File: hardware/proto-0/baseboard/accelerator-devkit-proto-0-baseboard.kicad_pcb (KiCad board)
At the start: 6 copper layers, 50 x 42 mm, 175 parts, among them J1 JTAG, J2 USB-C, J3 HDMI, J4 Qwiic I2C, J5 Pmod 1A, J6 Pmod 1B, J7 Display, J8 microSD-ST11-H, Q1 CSD13381F4, SW1 BUTTON1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

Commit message: Adding some ground stitch vias
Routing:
- net /SDRAM/~SDRAM_RESET: track 15.2 -> 13.3 mm
- net /SDRAM/SDRAM_D9: track 13.8 -> 14.4 mm
- net GND: vias 137 -> 148
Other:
- board text removed: "TODO: GND stitch vias"

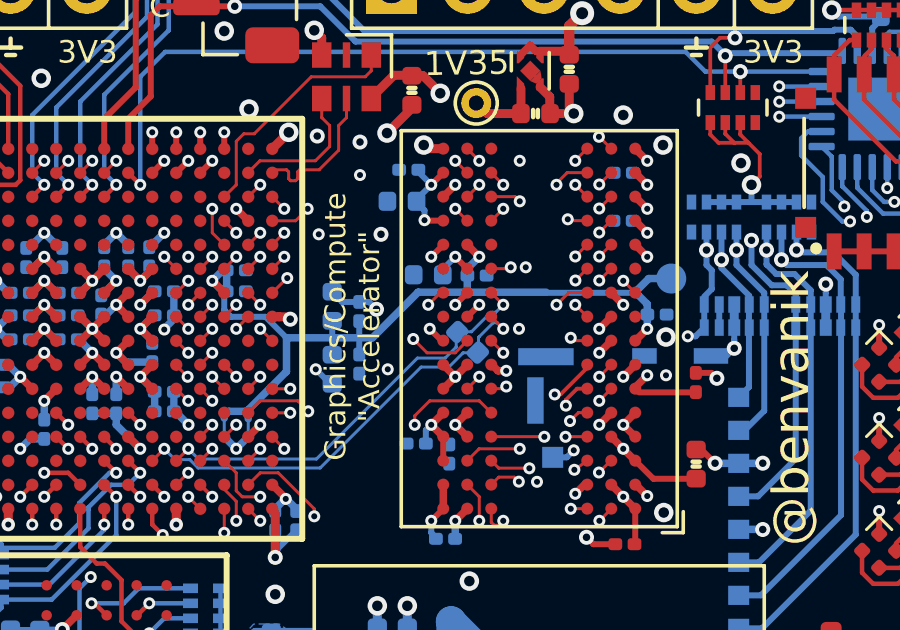
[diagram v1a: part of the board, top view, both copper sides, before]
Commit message: Thickening sDRAM_VREF traces
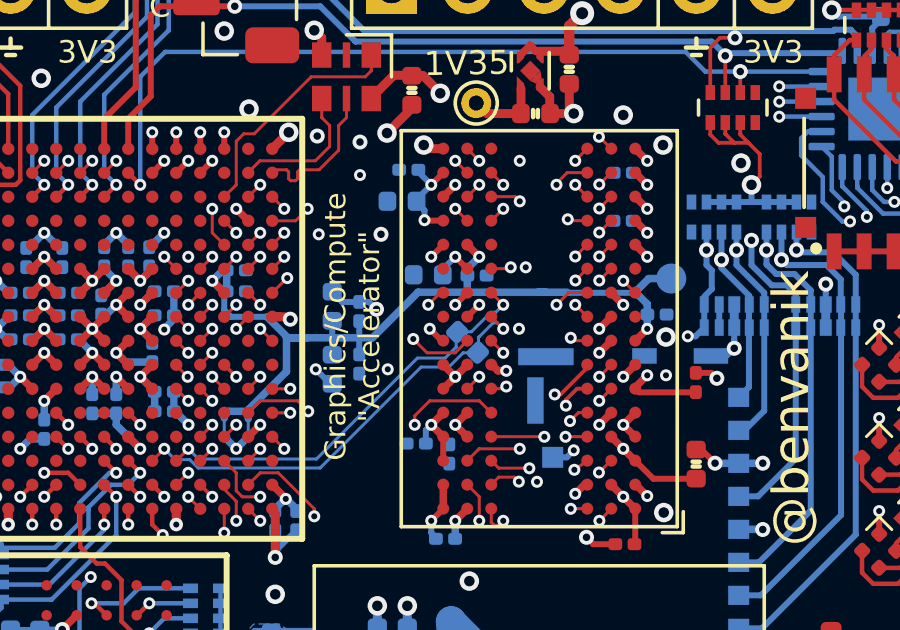
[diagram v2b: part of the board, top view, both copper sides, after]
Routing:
- net /SDRAM/VTT_REF: track 37.0 -> 39.6 mm
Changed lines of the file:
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@@
     (thickness 1.6)
     (drawings 37)
-    (tracks 3184)
+    (tracks 3192)
     (modules 175)
     (nets 346)
@@
       (dielectric_constraints yes)
     )
-    (last_trace_width 0.3)
+    (last_trace_width 0.2)
     (user_trace_width 0.09)
     (user_trace_width 0.1)
@@
   (gr_line (start 6.5 49) (end 51.5 49) (layer "Edge.Cuts") (width 0.05))
   (gr_line (start 4 9.5) (end 4 31) (layer "Edge.Cuts") (width 0.05))
+  (segment (start 38.97 22.03) (end 39.23 22.03) (width 0.25) (layer "B.Cu") (net 6))
+  (segment (start 39.95 22.05) (end 42.175 22.05) (width 0.2) (layer "B.Cu") (net 6))
+  (segment (start 39.25 22.05) (end 39.95 22.05) (width 0.2) (layer "B.Cu") (net 6))
+  (segment (start 34.96 22.03) (end 38.97 22.03) (width 0.25) (layer "B.Cu") (net 6))
+  (segment (start 38.97 22.03) (end 39.93 22.03) (width 0.25) (layer "B.Cu") (net 6))
+  (segment (start 30.575 23.55) (end 31.25 23.55) (width 0.25) (layer "B.Cu") (net 6))
+  (segment (start 30.625 23.55) (end 29.925 22.85) (width 0.25) (layer "B.Cu") (net 6))
+  (segment (start 31.25 23.55) (end 32.15 23.55) (width 0.25) (layer "B.Cu") (net 6))
+  (segment (start 31.25 23.55) (end 30.625 23.55) (width 0.25) (layer "B.Cu") (net 6))
+  (segment (start 30.575 23.55) (end 30.575 23.5) (width 0.2) (layer "B.Cu") (net 6))
+  (segment (start 30.575 23.5) (end 29.925 22.85) (width 0.2) (layer "B.Cu") (net 6))
+  (segment (start 29.925 22.85) (end 29.875 22.85) (width 0.2) (layer "B.Cu") (net 6))
   (via (at 28.5 13.325) (size 0.65) (drill 0.35) (layers "F.Cu" "B.Cu") (net 211))
   (via (at 27.55 48.1) (size 0.65) (drill 0.35) (layers "F.Cu" "B.Cu") (net 211))
@@
   (segment (start 34.94 24.49) (end 34.44 24.99) (width 0.127) (layer "In3.Cu") (net 105))
   (via (at 33.95 24.6) (size 0.4) (drill 0.2) (layers "F.Cu" "B.Cu") (net 211))
-  (segment (start 34.96 22.03) (end 39.23 22.03) (width 0.25) (layer "B.Cu") (net 6))
   (segment (start 33.44 23.55) (end 34.96 22.03) (width 0.25) (layer "B.Cu") (net 6))
   (segment (start 34.9 22.45) (end 35.3 22.45) (width 0.127) (layer "In2.Cu") (net 140))
@@
   (via (at 16.35 16.08) (size 0.5) (drill 0.25) (layers "F.Cu" "B.Cu") (net 1))
   (segment (start 16.35 16.08) (end 16.35 17.3125) (width 0.5) (layer "In3.Cu") (net 1))
-  (segment (start 39.25 22.05) (end 42.175 22.05) (width 0.2) (layer "B.Cu") (net 6))
   (segment (start 36.6 21.475) (end 36.6 22.01) (width 0.25) (layer "B.Cu") (net 6))
   (segment (start 36.6 22.01) (end 36.62 22.03) (width 0.25) (layer "B.Cu") (net 6))
@@
   (segment (start 28.45 22) (end 28.1 21.65) (width 0.25) (layer "B.Cu") (net 6))
   (segment (start 30.575 23.55) (end 30.575 24.675) (width 0.25) (layer "B.Cu") (net 6) (status 8000))
-  (segment (start 30.575 23.55) (end 29.875 22.85) (width 0.2) (layer "B.Cu") (net 6))
-  (segment (start 30.575 23.55) (end 32.15 23.55) (width 0.25) (layer "B.Cu") (net 6))
   (segment (start 33 22.355) (end 32.43 22.355) (width 0.2) (layer "B.Cu") (net 211))
   (segment (start 32.43 22.355) (end 32.1 22.025) (width 0.2) (layer "B.Cu") (net 211))

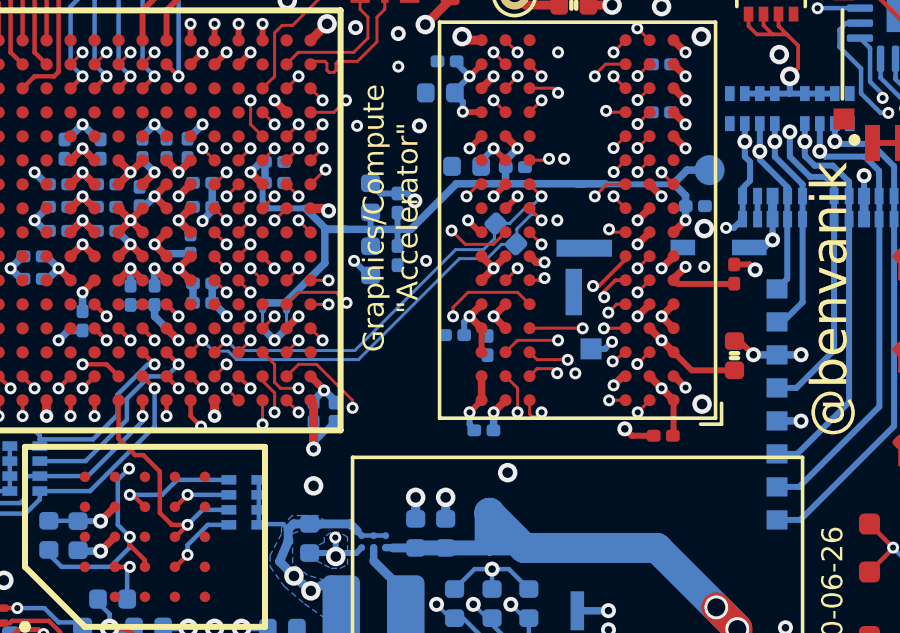
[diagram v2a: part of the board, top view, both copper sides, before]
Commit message: Length matching SDRAM upper byte
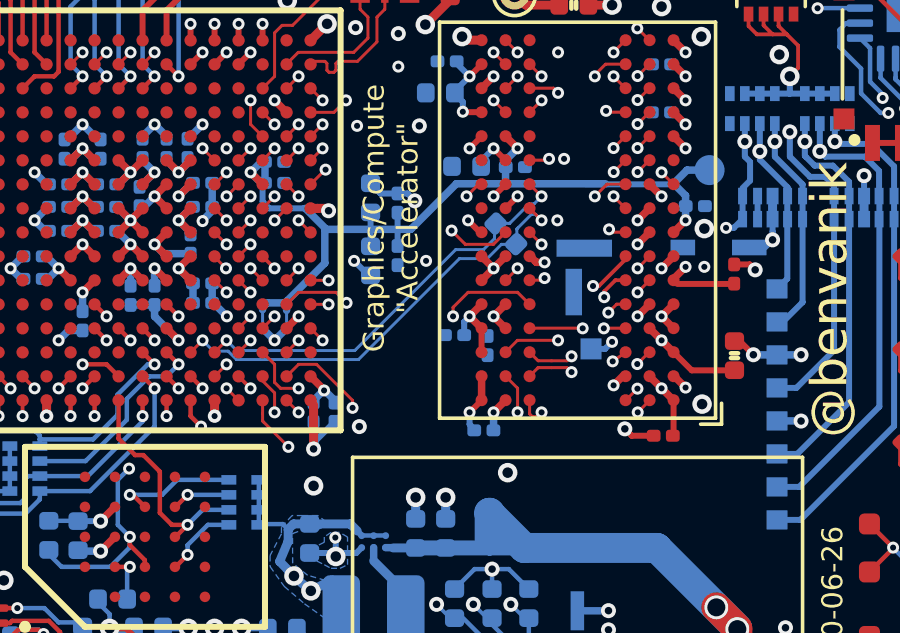
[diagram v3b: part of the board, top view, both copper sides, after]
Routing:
- net /SDRAM/SDRAM_D14: track 9.56 -> 15.0 mm
- net /SDRAM/SDRAM_D12: track 11.7 -> 15.0 mm
- net /SDRAM/SDRAM_D15: track 12.4 -> 15.0 mm
- net /SDRAM/SDRAM_D10: track 13.2 -> 15.0 mm
- net /SDRAM/SDRAM_UDQS-: track 13.3 -> 15.0 mm
- net /SDRAM/SDRAM_UDM: track 13.5 -> 15.0 mm
- net /SDRAM/SDRAM_UDQS+: track 13.6 -> 15.0 mm
- net /SDRAM/VTT_REF: track 39.6 -> 38.7 mm
- net /SDRAM/SDRAM_D8: track 14.2 -> 15.0 mm
- net /SDRAM/SDRAM_D9: track 14.4 -> 15.0 mm

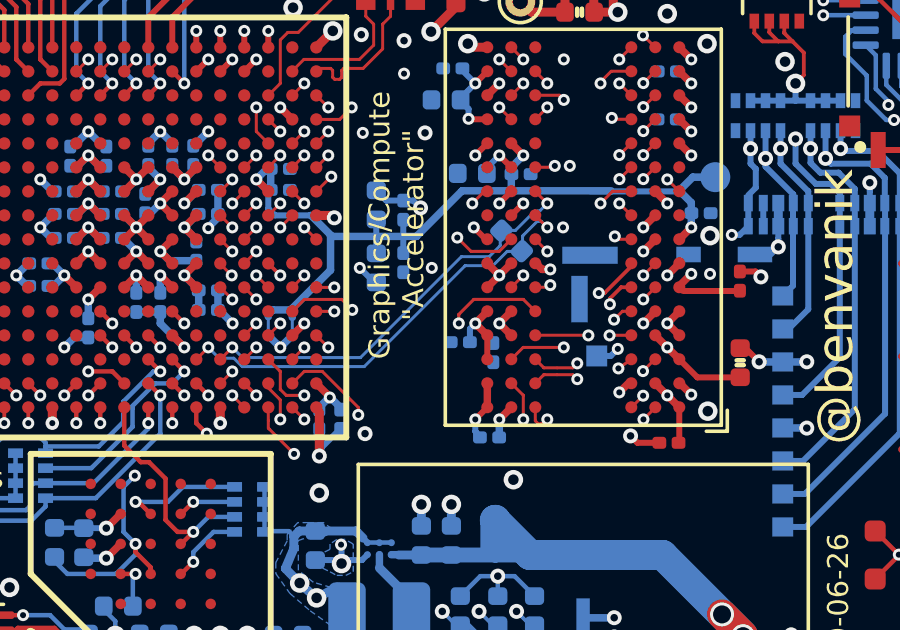
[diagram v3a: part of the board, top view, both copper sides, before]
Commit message: Length matching SDRAM lower byte
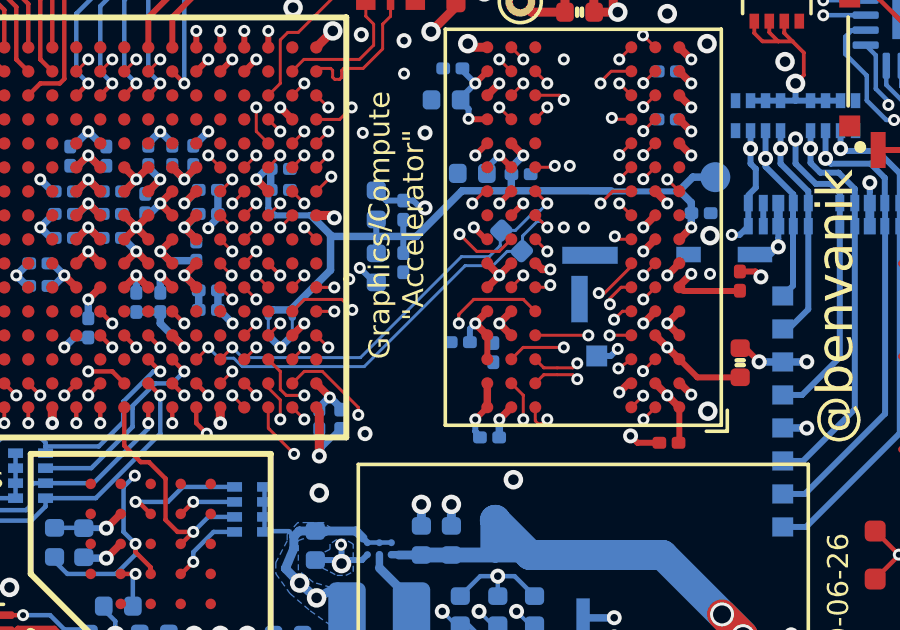
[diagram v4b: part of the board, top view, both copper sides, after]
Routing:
- net /SDRAM/SDRAM_D1: track 8.64 -> 15.0 mm
- net /SDRAM/SDRAM_D3: track 8.84 -> 15.0 mm
- net /SDRAM/SDRAM_D5: track 9.61 -> 15.0 mm
- net /SDRAM/SDRAM_D7: track 11.2 -> 15.0 mm
- net /SDRAM/SDRAM_LDQS+: track 11.6 -> 15.0 mm
- net /SDRAM/SDRAM_LDM: track 11.9 -> 15.0 mm
- net /SDRAM/SDRAM_D0: track 12.7 -> 15.0 mm
- net /SDRAM/SDRAM_LDQS-: track 12.8 -> 15.0 mm
- net /SDRAM/SDRAM_D2: track 13.5 -> 15.0 mm
- net /SDRAM/SDRAM_D4: track 14.5 -> 15.0 mm
- net GND: vias 148 -> 149
